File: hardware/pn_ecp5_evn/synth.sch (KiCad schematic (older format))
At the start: 32 parts, among them J201 Conn_Coaxial, U201 VEMI65AB-HCI, U202 LMX2594

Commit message: first pass footprint assignment on pn r0
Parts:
- C201, C203, C208, C210, C218, C219, C220: footprint (none) -> Capacitor_SMD:C_0603_1608Metric
- C202, C204, C205, C206, C207, C209, C211, C212, C213, C214, C215, C216, C217: footprint (none) -> Capacitor_SMD:C_0402_1005Metric
- D201: value LED_Small -> RED; footprint (none) -> LED_SMD:LED_0603_1608Metric
- J201: footprint (none) -> Connector_Coaxial:SMA_Molex_73251-1153_EdgeMount_Horizontal
- R201: value R_Small -> 10k; footprint (none) -> Resistor_SMD:R_0402_1005Metric
- R202, R203, R204, R205, R206, R207, R208: footprint (none) -> Resistor_SMD:R_0402_1005Metric
- U201: footprint (none) -> vna:LLP2513-13L
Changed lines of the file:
@@
 F 0 "C214" H 6592 2146 50  0000 L CNN
 F 1 "1 uF" H 6592 2055 50  0000 L CNN
-F 2 "" H 6500 2100 50  0001 C CNN
+F 2 "Capacitor_SMD:C_0402_1005Metric" H 6500 2100 50  0001 C CNN
 F 3 "~" H 6500 2100 50  0001 C CNN
 	1    6500 2100
@@
 F 0 "C210" H 3992 5346 50  0000 L CNN
 F 1 "10 uF" H 3992 5255 50  0000 L CNN
-F 2 "" H 3900 5300 50  0001 C CNN
+F 2 "Capacitor_SMD:C_0603_1608Metric" H 3900 5300 50  0001 C CNN
 F 3 "~" H 3900 5300 50  0001 C CNN
 	1    3900 5300
@@
 F 0 "C208" H 3592 5346 50  0000 L CNN
 F 1 "10 uF" H 3592 5255 50  0000 L CNN
-F 2 "" H 3500 5300 50  0001 C CNN
+F 2 "Capacitor_SMD:C_0603_1608Metric" H 3500 5300 50  0001 C CNN
 F 3 "~" H 3500 5300 50  0001 C CNN
 	1    3500 5300
@@
 F 0 "C205" H 3192 5346 50  0000 L CNN
 F 1 "1 uF" H 3192 5255 50  0000 L CNN
-F 2 "" H 3100 5300 50  0001 C CNN
+F 2 "Capacitor_SMD:C_0402_1005Metric" H 3100 5300 50  0001 C CNN
 F 3 "~" H 3100 5300 50  0001 C CNN
 	1    3100 5300
@@
 F 0 "C204" H 2792 5346 50  0000 L CNN
 F 1 "1 uF" H 2792 5255 50  0000 L CNN
-F 2 "" H 2700 5300 50  0001 C CNN
+F 2 "Capacitor_SMD:C_0402_1005Metric" H 2700 5300 50  0001 C CNN
 F 3 "~" H 2700 5300 50  0001 C CNN
 	1    2700 5300
@@
 F 0 "C203" H 2392 5346 50  0000 L CNN
 F 1 "10 uF" H 2392 5255 50  0000 L CNN
-F 2 "" H 2300 5300 50  0001 C CNN
+F 2 "Capacitor_SMD:C_0603_1608Metric" H 2300 5300 50  0001 C CNN
 F 3 "~" H 2300 5300 50  0001 C CNN
 	1    2300 5300
@@
 F 0 "C202" H 1992 5346 50  0000 L CNN
 F 1 "1 uF" H 1992 5255 50  0000 L CNN
-F 2 "" H 1900 5300 50  0001 C CNN
+F 2 "Capacitor_SMD:C_0402_1005Metric" H 1900 5300 50  0001 C CNN
 F 3 "~" H 1900 5300 50  0001 C CNN
 	1    1900 5300
@@
 F 0 "C201" H 1592 5346 50  0000 L CNN
 F 1 "10 uF" H 1592 5255 50  0000 L CNN
-F 2 "" H 1500 5300 50  0001 C CNN
+F 2 "Capacitor_SMD:C_0603_1608Metric" H 1500 5300 50  0001 C CNN
 F 3 "~" H 1500 5300 50  0001 C CNN
 	1    1500 5300
@@
 F 0 "C216" H 6942 2146 50  0000 L CNN
 F 1 "100 nF" H 6942 2055 50  0000 L CNN
-F 2 "" H 6850 2100 50  0001 C CNN
+F 2 "Capacitor_SMD:C_0402_1005Metric" H 6850 2100 50  0001 C CNN
 F 3 "~" H 6850 2100 50  0001 C CNN
 	1    6850 2100
@@
 F 0 "C213" H 6142 2146 50  0000 L CNN
 F 1 "1 uF" H 6142 2055 50  0000 L CNN
-F 2 "" H 6050 2100 50  0001 C CNN
+F 2 "Capacitor_SMD:C_0402_1005Metric" H 6050 2100 50  0001 C CNN
 F 3 "~" H 6050 2100 50  0001 C CNN
 	1    6050 2100
@@
 F 0 "C211" H 4192 2146 50  0000 L CNN
 F 1 "1 uF" H 4192 2055 50  0000 L CNN
-F 2 "" H 4100 2100 50  0001 C CNN
+F 2 "Capacitor_SMD:C_0402_1005Metric" H 4100 2100 50  0001 C CNN
 F 3 "~" H 4100 2100 50  0001 C CNN
 	1    4100 2100
@@
 F 0 "C212" H 4542 2146 50  0000 L CNN
 F 1 "1 uF" H 4542 2055 50  0000 L CNN
-F 2 "" H 4450 2100 50  0001 C CNN
+F 2 "Capacitor_SMD:C_0402_1005Metric" H 4450 2100 50  0001 C CNN
 F 3 "~" H 4450 2100 50  0001 C CNN
 	1    4450 2100
@@
 F 0 "C209" H 3842 2146 50  0000 L CNN
 F 1 "1 uF" H 3842 2055 50  0000 L CNN
-F 2 "" H 3750 2100 50  0001 C CNN
+F 2 "Capacitor_SMD:C_0402_1005Metric" H 3750 2100 50  0001 C CNN
 F 3 "~" H 3750 2100 50  0001 C CNN
 	1    3750 2100
@@
 U 1 1 5F2DB5AF
 P 3500 4100
-F 0 "C206" V 3450 4000 50  0000 C CNN
+F 0 "C206" V 3450 3950 50  0000 C CNN
 F 1 "10 nF" V 3450 4250 50  0000 C CNN
-F 2 "" H 3500 4100 50  0001 C CNN
+F 2 "Capacitor_SMD:C_0402_1005Metric" H 3500 4100 50  0001 C CNN
 F 3 "~" H 3500 4100 50  0001 C CNN
 	1    3500 4100
@@
 U 1 1 5F2DBC0F
 P 3500 4250
-F 0 "C207" V 3450 4150 50  0000 C CNN
+F 0 "C207" V 3450 4100 50  0000 C CNN
 F 1 "10 nF" V 3450 4400 50  0000 C CNN
-F 2 "" H 3500 4250 50  0001 C CNN
+F 2 "Capacitor_SMD:C_0402_1005Metric" H 3500 4250 50  0001 C CNN
 F 3 "~" H 3500 4250 50  0001 C CNN
 	1    3500 4250
@@
 U 1 1 5F2DF2DA
 P 3150 4250
-F 0 "R202" H 3209 4296 50  0000 L CNN
-F 1 "50" H 3209 4205 50  0000 L CNN
-F 2 "" H 3150 4250 50  0001 C CNN
+F 0 "R202" V 3050 4300 50  0000 L CNN
+F 1 "50" V 3050 4150 50  0000 L CNN
+F 2 "Resistor_SMD:R_0402_1005Metric" H 3150 4250 50  0001 C CNN
 F 3 "~" H 3150 4250 50  0001 C CNN
 	1    3150 4250
@@
 F 0 "U201" H 3050 3715 50  0000 C CNN
 F 1 "VEMI65AB-HCI" H 3050 3624 50  0000 C CNN
-F 2 "" H 3100 3000 50  0001 C CNN
+F 2 "vna:LLP2513-13L" H 3100 3000 50  0001 C CNN
 F 3 "" H 3100 3000 50  0001 C CNN
 	1    3050 3200
@@
 F 0 "R203" V 4000 3650 50  0000 C CNN
 F 1 "0" V 4000 3550 50  0000 C CNN
-F 2 "" H 3900 3600 50  0001 C CNN
+F 2 "Resistor_SMD:R_0402_1005Metric" H 3900 3600 50  0001 C CNN
 F 3 "~" H 3900 3600 50  0001 C CNN
 	1    3900 3600
@@
 F 0 "C215" H 6692 5196 50  0000 L CNN
 F 1 "1800 pF" H 6692 5105 50  0000 L CNN
-F 2 "" H 6600 5150 50  0001 C CNN
+F 2 "Capacitor_SMD:C_0402_1005Metric" H 6600 5150 50  0001 C CNN
 F 3 "~" H 6600 5150 50  0001 C CNN
 	1    6600 5150
@@
 F 0 "C218" H 8742 5196 50  0000 L CNN
 F 1 "DNI" H 8742 5105 50  0000 L CNN
-F 2 "" H 8650 5150 50  0001 C CNN
+F 2 "Capacitor_SMD:C_0603_1608Metric" H 8650 5150 50  0001 C CNN
 F 3 "~" H 8650 5150 50  0001 C CNN
 	1    8650 5150
@@
 F 0 "R204" H 7209 5146 50  0000 L CNN
 F 1 "47k" H 7209 5055 50  0000 L CNN
-F 2 "" H 7150 5100 50  0001 C CNN
+F 2 "Resistor_SMD:R_0402_1005Metric" H 7150 5100 50  0001 C CNN
 F 3 "~" H 7150 5100 50  0001 C CNN
 	1    7150 5100
@@
 F 0 "C217" H 7592 5546 50  0000 L CNN
 F 1 "10 nF" H 7592 5455 50  0000 L CNN
-F 2 "" H 7500 5500 50  0001 C CNN
+F 2 "Capacitor_SMD:C_0402_1005Metric" H 7500 5500 50  0001 C CNN
 F 3 "~" H 7500 5500 50  0001 C CNN
 	1    7500 5500
@@
 F 0 "R205" H 7209 5546 50  0000 L CNN
 F 1 "47k" H 7209 5455 50  0000 L CNN
-F 2 "" H 7150 5500 50  0001 C CNN
+F 2 "Resistor_SMD:R_0402_1005Metric" H 7150 5500 50  0001 C CNN
 F 3 "~" H 7150 5500 50  0001 C CNN
 	1    7150 5500
@@
 F 0 "R207" V 9296 4950 50  0000 C CNN
 F 1 "0k" V 9205 4950 50  0000 C CNN
-F 2 "" H 9100 4950 50  0001 C CNN
+F 2 "Resistor_SMD:R_0402_1005Metric" H 9100 4950 50  0001 C CNN
 F 3 "~" H 9100 4950 50  0001 C CNN
 	1    9100 4950
@@
 F 0 "C219" H 9492 5196 50  0000 L CNN
 F 1 "68 nF" H 9492 5105 50  0000 L CNN
-F 2 "" H 9400 5150 50  0001 C CNN
+F 2 "Capacitor_SMD:C_0603_1608Metric" H 9400 5150 50  0001 C CNN
 F 3 "~" H 9400 5150 50  0001 C CNN
 	1    9400 5150
@@
 F 0 "R208" H 9459 5496 50  0000 L CNN
 F 1 "68" H 9459 5405 50  0000 L CNN
-F 2 "" H 9400 5450 50  0001 C CNN
+F 2 "Resistor_SMD:R_0402_1005Metric" H 9400 5450 50  0001 C CNN
 F 3 "~" H 9400 5450 50  0001 C CNN
 	1    9400 5450
@@
 F 0 "C220" H 9992 5196 50  0000 L CNN
 F 1 "390 pF" H 9992 5105 50  0000 L CNN
-F 2 "" H 9900 5150 50  0001 C CNN
+F 2 "Capacitor_SMD:C_0603_1608Metric" H 9900 5150 50  0001 C CNN
 F 3 "~" H 9900 5150 50  0001 C CNN
 	1    9900 5150
@@
 F 0 "J201" H 8850 4125 50  0000 L CNN
 F 1 "Conn_Coaxial" H 8850 4034 50  0000 L CNN
-F 2 "" H 8750 4150 50  0001 C CNN
+F 2 "Connector_Coaxial:SMA_Molex_73251-1153_EdgeMount_Horizontal" H 8750 4150 50  0001 C CNN
 F 3 " ~" H 8750 4150 50  0001 C CNN
 	1    8750 4150
@@
 F 0 "R206" V 7800 5350 50  0000 L CNN
 F 1 "0" V 7800 5200 50  0000 L CNN
-F 2 "" H 7700 5300 50  0001 C CNN
+F 2 "Resistor_SMD:R_0402_1005Metric" H 7700 5300 50  0001 C CNN
 F 3 "~" H 7700 5300 50  0001 C CNN
 	1    7700 5300
@@
 P 1250 3550
 F 0 "D201" V 1296 3480 50  0000 R CNN
-F 1 "LED_Small" V 1205 3480 50  0000 R CNN
-F 2 "" V 1250 3550 50  0001 C CNN
+F 1 "RED" V 1205 3480 50  0000 R CNN
+F 2 "LED_SMD:LED_0603_1608Metric" V 1250 3550 50  0001 C CNN
 F 3 "~" V 1250 3550 50  0001 C CNN
 	1    1250 3550
@@
 P 1250 3950
 F 0 "R201" H 1309 3996 50  0000 L CNN
-F 1 "R_Small" H 1309 3905 50  0000 L CNN
-F 2 "" H 1250 3950 50  0001 C CNN
+F 1 "10k" H 1309 3905 50  0000 L CNN
+F 2 "Resistor_SMD:R_0402_1005Metric" H 1250 3950 50  0001 C CNN
 F 3 "~" H 1250 3950 50  0001 C CNN
 	1    1250 3950

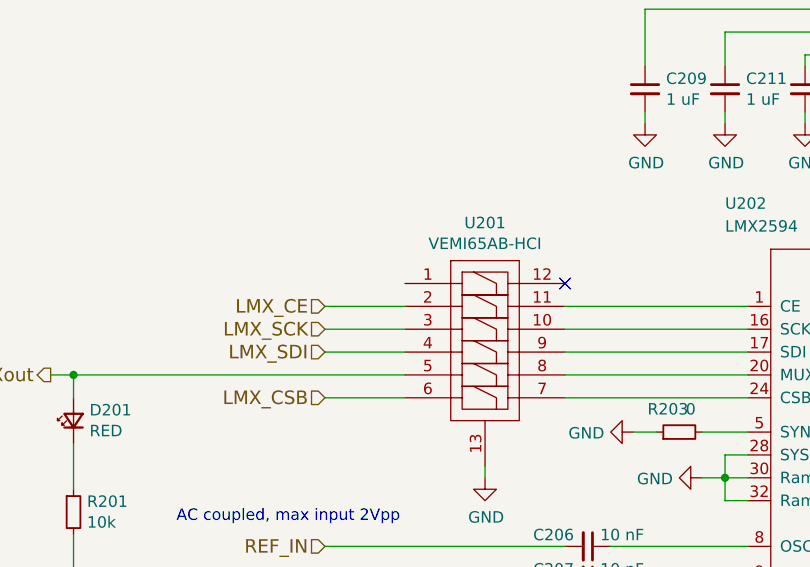
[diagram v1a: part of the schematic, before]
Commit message: started component placement on phase noise analyzer
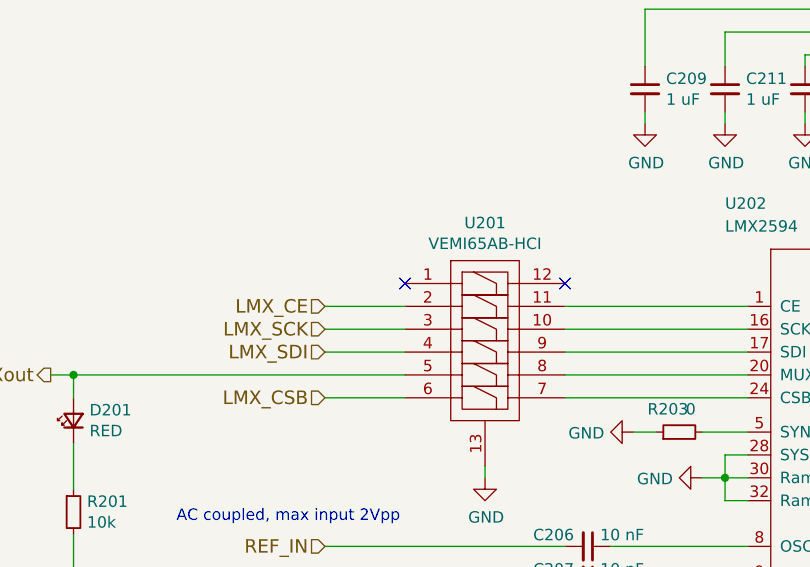
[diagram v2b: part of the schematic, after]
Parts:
- J201: footprint Connector_Coaxial:SMA_Molex_73251-1153_EdgeMount_Horizontal -> vna:SMA_Molex_73251-1153_OSHFR408
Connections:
- no-connect marks 1 -> 2
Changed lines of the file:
@@
 F 0 "J201" H 8850 4125 50  0000 L CNN
 F 1 "Conn_Coaxial" H 8850 4034 50  0000 L CNN
-F 2 "Connector_Coaxial:SMA_Molex_73251-1153_EdgeMount_Horizontal" H 8750 4150 50  0001 C CNN
+F 2 "vna:SMA_Molex_73251-1153_OSHFR408" H 8750 4150 50  0001 C CNN
 F 3 " ~" H 8750 4150 50  0001 C CNN
 	1    8750 4150
@@
 Wire Wire Line
 	1150 3350 1250 3350
+NoConn ~ 2700 2950
 $EndSCHEMATC

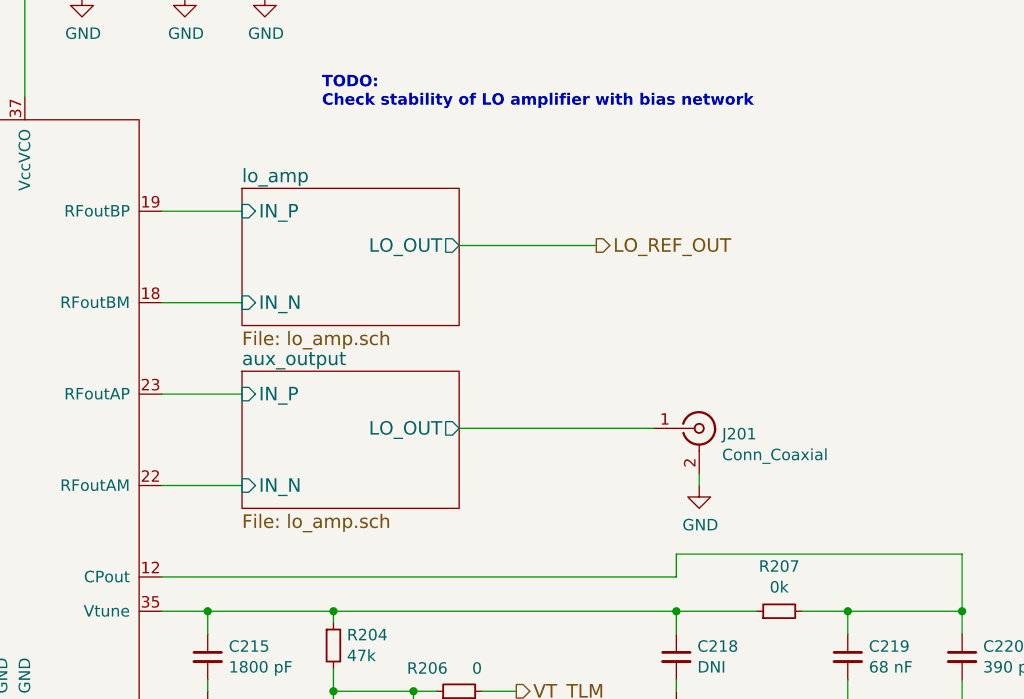
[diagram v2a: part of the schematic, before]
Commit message: component placement on phase noise downconverter
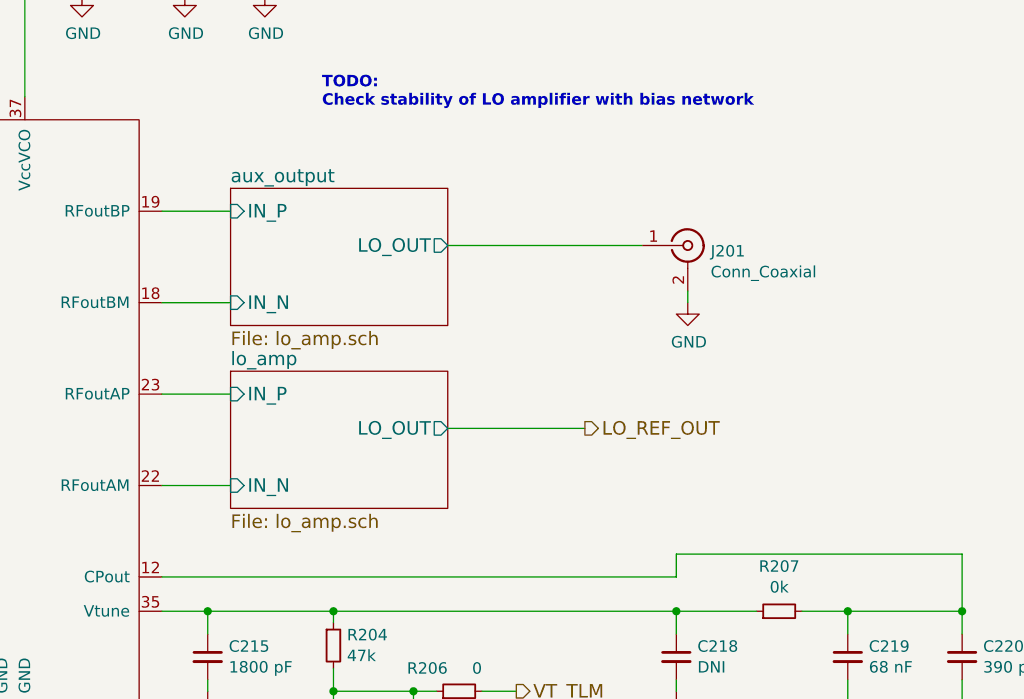
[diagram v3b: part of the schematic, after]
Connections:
- net aux_output/IN_N: now also U202.18 (RFoutBM); no longer U202.22 (RFoutAM)
- net aux_output/IN_P: now also U202.19 (RFoutBP); no longer U202.23 (RFoutAP)
- net lo_amp/IN_N: now also U202.22 (RFoutAM); no longer U202.18 (RFoutBM)
- net lo_amp/IN_P: now also U202.23 (RFoutAP); no longer U202.19 (RFoutBP)
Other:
- moved on the sheet: J201
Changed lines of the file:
@@
 Connection ~ 9900 4950
 $Sheet
-S 6750 3100 950  600
+S 6700 3900 950  600
 U 5F5F4CC2
 F0 "lo_amp" 59
 F1 "lo_amp.sch" 59
-F2 "LO_OUT" O R 7700 3350 59
-F3 "IN_P" I L 6750 3200 59
-F4 "IN_N" I L 6750 3600 59
+F2 "LO_OUT" O R 7650 4150 59
+F3 "IN_P" I L 6700 4000 59
+F4 "IN_N" I L 6700 4400 59
 $EndSheet
 $Sheet
-S 6750 3900 950  600
+S 6700 3100 950  600
 U 5F6340DA
 F0 "aux_output" 59
 F1 "lo_amp.sch" 59
-F2 "LO_OUT" O R 7700 4150 59
-F3 "IN_P" I L 6750 4000 59
-F4 "IN_N" I L 6750 4400 59
+F2 "LO_OUT" O R 7650 3350 59
+F3 "IN_P" I L 6700 3200 59
+F4 "IN_N" I L 6700 3600 59
 $EndSheet
-Wire Wire Line
-	6400 4000 6750 4000
-Wire Wire Line
-	6400 4400 6750 4400
-Wire Wire Line
-	6400 3200 6750 3200
 $Comp
 L Connector:Conn_Coaxial J201
 U 1 1 5F1FE536
-P 8750 4150
-F 0 "J201" H 8850 4125 50  0000 L CNN
-F 1 "Conn_Coaxial" H 8850 4034 50  0000 L CNN
-F 2 "vna:SMA_Molex_73251-1153_OSHFR408" H 8750 4150 50  0001 C CNN
-F 3 " ~" H 8750 4150 50  0001 C CNN
-	1    8750 4150
+P 8700 3350
+F 0 "J201" H 8800 3325 50  0000 L CNN
+F 1 "Conn_Coaxial" H 8800 3234 50  0000 L CNN
+F 2 "vna:SMA_Molex_73251-1153_OSHFR408" H 8700 3350 50  0001 C CNN
+F 3 " ~" H 8700 3350 50  0001 C CNN
+	1    8700 3350
 	1    0    0    -1
 $EndComp
@@
 L power:GND #PWR0141
 U 1 1 5F1FE53C
-P 8750 4400
-F 0 "#PWR0141" H 8750 4150 50  0001 C CNN
-F 1 "GND" H 8755 4227 50  0000 C CNN
-F 2 "" H 8750 4400 50  0001 C CNN
-F 3 "" H 8750 4400 50  0001 C CNN
-	1    8750 4400
+P 8700 3600
+F 0 "#PWR0141" H 8700 3350 50  0001 C CNN
+F 1 "GND" H 8705 3427 50  0000 C CNN
+F 2 "" H 8700 3600 50  0001 C CNN
+F 3 "" H 8700 3600 50  0001 C CNN
+	1    8700 3600
 	1    0    0    -1
 $EndComp
 Wire Wire Line
-	8750 4400 8750 4350
+	8700 3600 8700 3550
 Wire Wire Line
-	7700 3350 8300 3350
-Text HLabel 8300 3350 2    59   Output ~ 0
+	7650 4150 8250 4150
+Text HLabel 8250 4150 2    59   Output ~ 0
 LO_REF_OUT
-Wire Wire Line
-	6400 3600 6750 3600
 Wire Wire Line
 	6400 4800 8650 4800
@@
 AC coupled, max input 2Vpp
 Wire Wire Line
-	7700 4150 8550 4150
+	7650 3350 8500 3350
 $Comp
 L Device:LED_Small D201
@@
 	1150 3350 1250 3350
 NoConn ~ 2700 2950
+Wire Wire Line
+	6400 4000 6700 4000
+Wire Wire Line
+	6400 4400 6700 4400
+Wire Wire Line
+	6400 3600 6700 3600
+Wire Wire Line
+	6400 3200 6700 3200
 $EndSCHEMATC

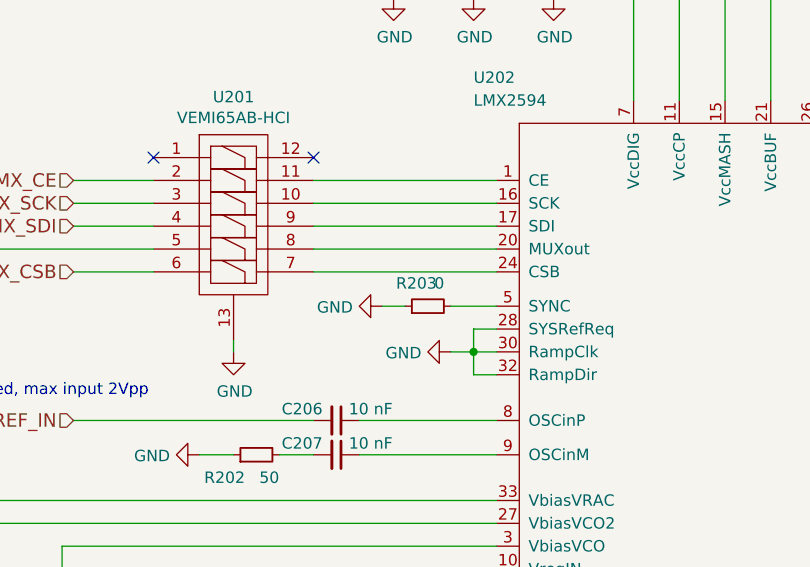
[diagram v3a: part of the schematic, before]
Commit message: checked stability of LO amplifier, started migen project, added more flexibility for active filtering on baseband path
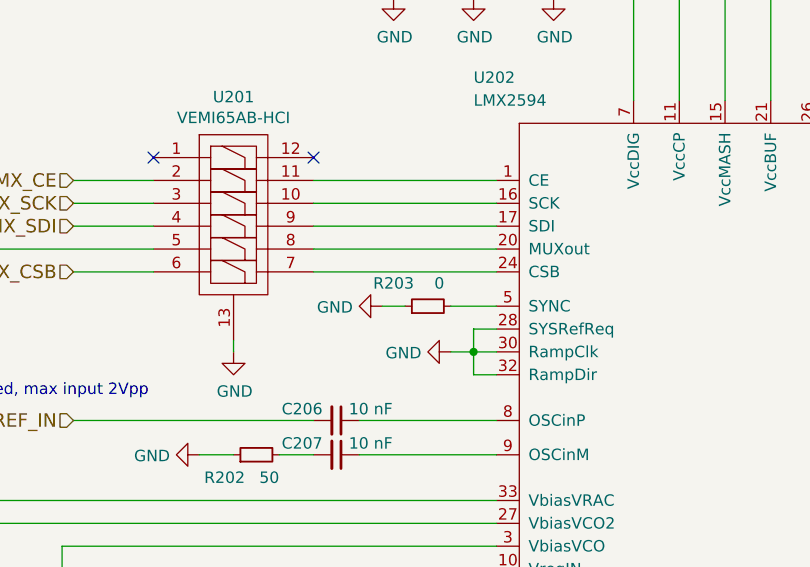
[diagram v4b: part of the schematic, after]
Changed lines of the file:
@@
 U 1 1 5F33A873
 P 3900 3600
-F 0 "R203" V 4000 3650 50  0000 C CNN
+F 0 "R203" V 4000 3750 50  0000 C CNN
 F 1 "0" V 4000 3550 50  0000 C CNN
 F 2 "Resistor_SMD:R_0402_1005Metric" H 3900 3600 50  0001 C CNN

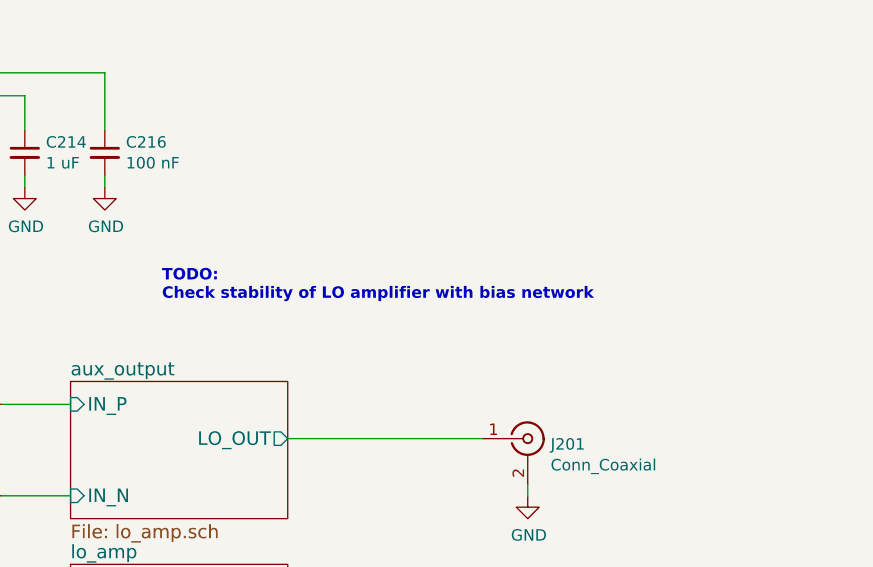
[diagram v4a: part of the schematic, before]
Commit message: final layout cleanup, ordered phase noise downconverter boards
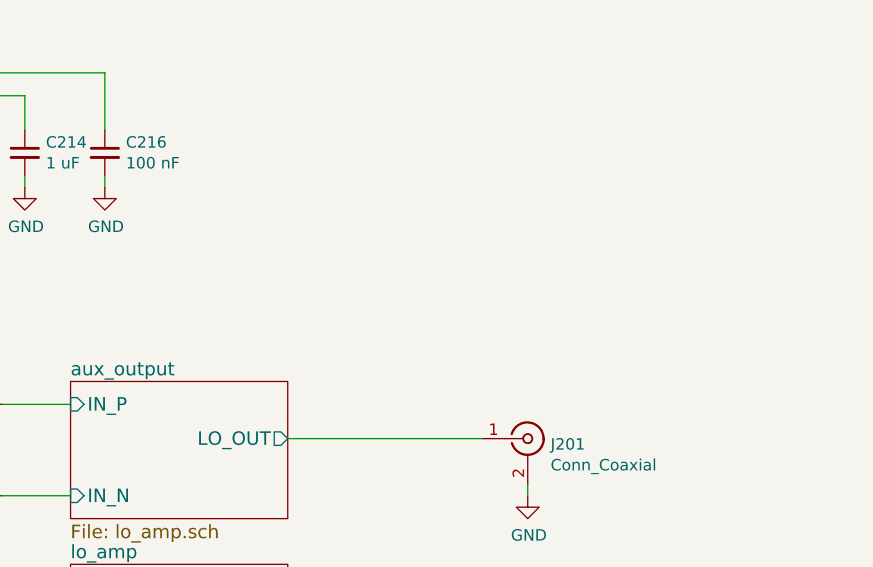
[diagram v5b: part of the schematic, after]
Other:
- note removed: "TODO:\nCheck stability of LO amplifier with bias network"
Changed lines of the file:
@@
 Wire Wire Line
 	7800 5300 7950 5300
-Text Notes 7100 2750 0    50   ~ 10
-TODO:\nCheck stability of LO amplifier with bias network
 Text Notes 1700 4000 0    50   ~ 0
 AC coupled, max input 2Vpp
